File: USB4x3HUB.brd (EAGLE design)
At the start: 80 x 90 mm, 115 parts, among them IC1 TUSB2036, IC10 SN74LVC1G139DCTR, IC2 FSUSB74MPX, IC3 TPS2041C, IC4 TPS2041C, IC5 TPS2041C, IC6 3.3V, IC7 5V, IC8 5V, IC9 5V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

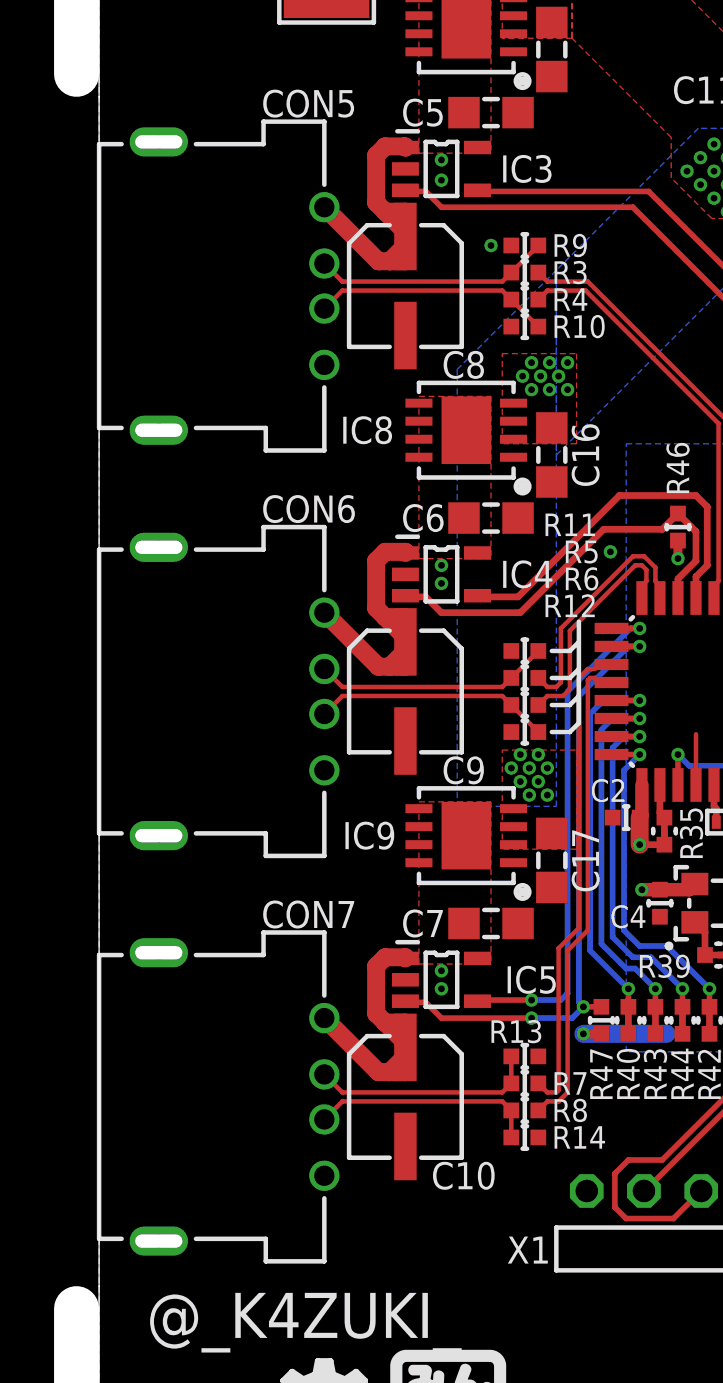
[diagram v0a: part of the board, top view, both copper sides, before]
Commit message: [ PCB ] library update and related fix
- CON5-7 pinout mistake fixed in library
  - move C8-10 to followw this change
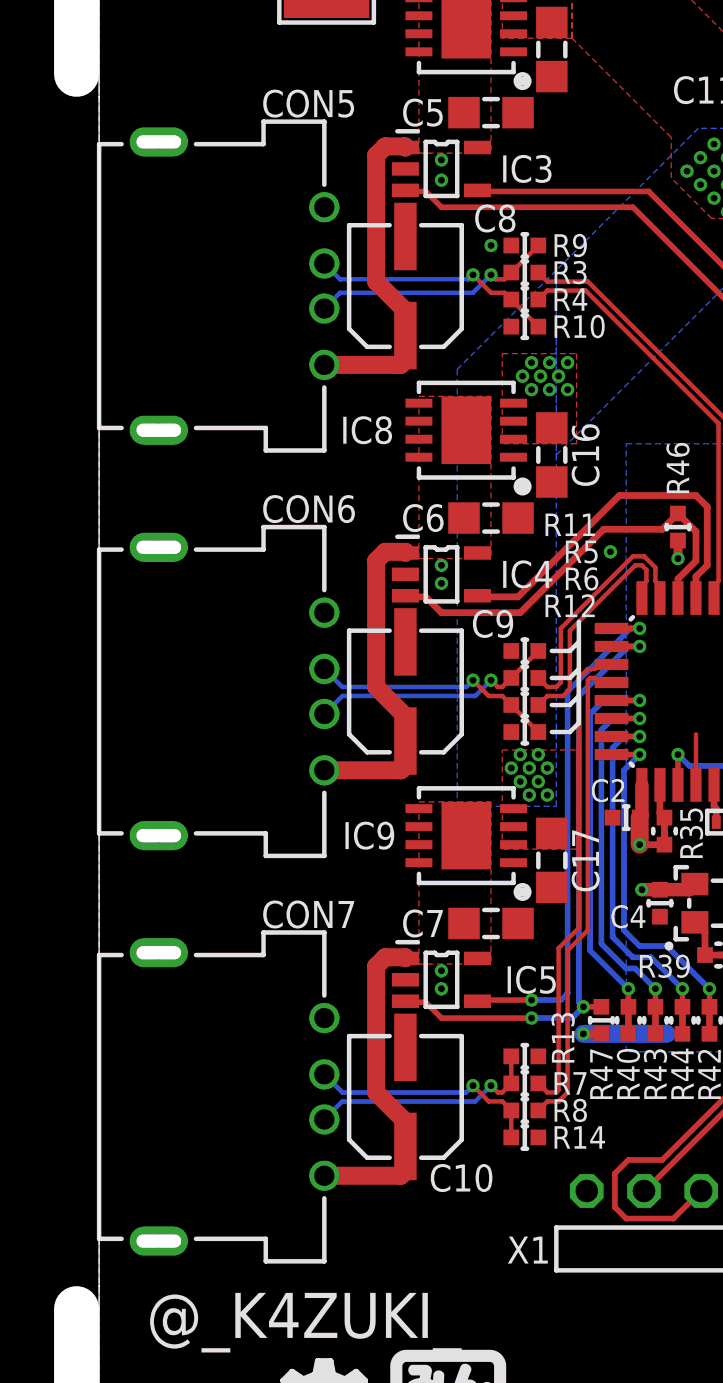
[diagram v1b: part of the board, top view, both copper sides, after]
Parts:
- turned C10 to 0 degrees
- turned C8 to 0 degrees
- turned C9 to 0 degrees
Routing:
- net N$12: track 14.1 -> 14.8 mm
- net N$13: track 14.1 -> 14.8 mm
- net N$11: track 14.2 -> 14.9 mm
- net N$27: track 10.00 -> 10.4 mm, vias 0 -> 1
- net N$26: track 10.00 -> 10.4 mm, vias 0 -> 1
- net N$23: track 10.5 -> 10.9 mm, vias 0 -> 1
- net N$22: track 10.5 -> 10.9 mm, vias 0 -> 1
- net N$19: track 10.5 -> 10.8 mm, vias 0 -> 1
- net N$18: track 10.5 -> 10.8 mm, vias 0 -> 1

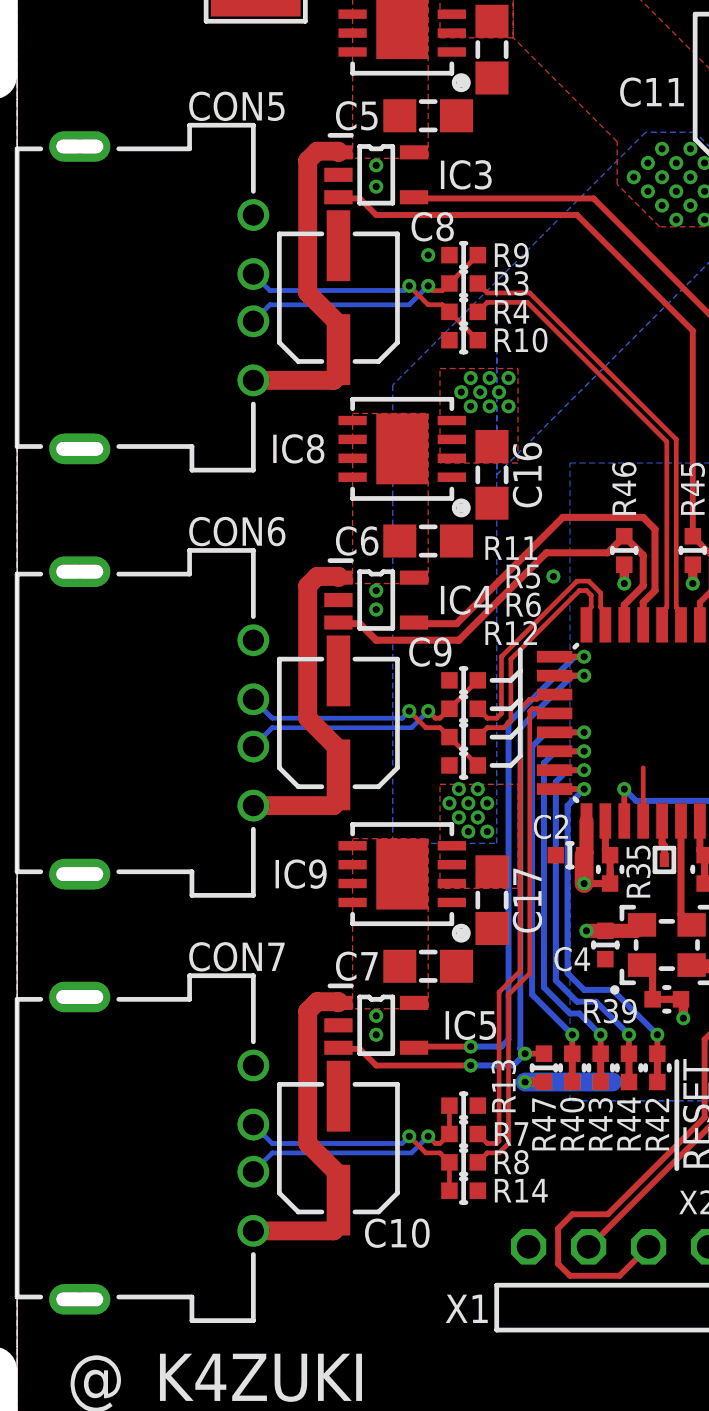
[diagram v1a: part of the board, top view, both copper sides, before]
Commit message: [ PCB ] move C8-10; shift USB downstream traces
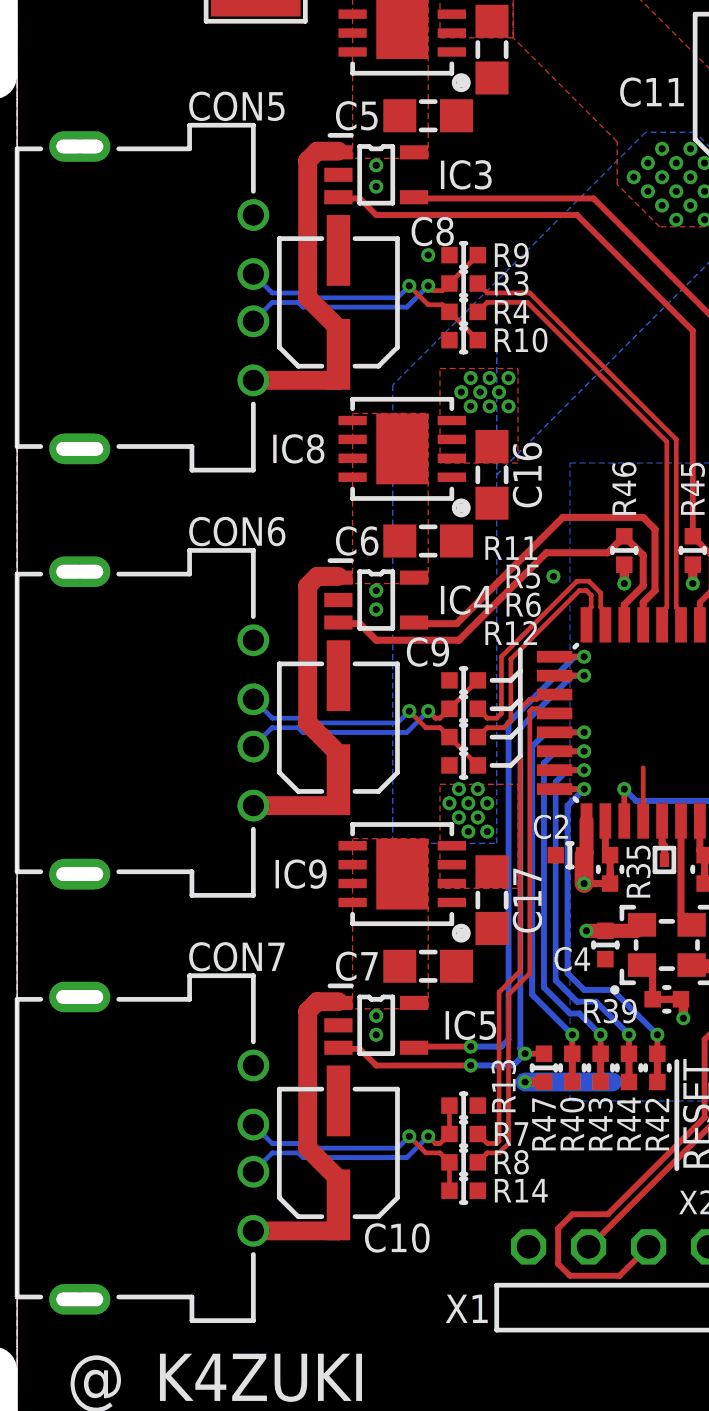
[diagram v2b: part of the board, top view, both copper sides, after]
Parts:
- moved C8 0.20 mm to (25.6, 62.8)
- moved C9 0.20 mm to (25.6, 44.8)
- moved C10 0.20 mm to (25.6, 26.8)

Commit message: [ BRD ] fix clock mode
- 48M source used while 6M source selected for IC
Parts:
- moved R38 0.10 mm to (41.0, 38.8)
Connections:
- net 3.3V: now also R38.1, R38.2
- net GND: no longer R38.1, R38.2
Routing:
- net 3.3V: track 63.7 -> 65.1 mm, vias 28 -> 29
- net GND: track 17.7 -> 16.4 mm
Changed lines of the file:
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@@
 <attribute name="VALUE" x="28.3" y="38.6" size="1.2" layer="27" ratio="17" rot="R90" align="center"/>
 </element>
-<element name="R38" library="mylib" package="R0402SHORT" value="" x="41.1" y="38.8" smashed="yes" rot="R90">
+<element name="R38" library="mylib" package="R0402SHORT" value="" x="41" y="38.8" smashed="yes" rot="R90">
 <attribute name="NAME" x="42.3" y="38.8" size="1" layer="25" font="vector" ratio="20" rot="R90" align="center"/>
-<attribute name="VALUE" x="41.1" y="38.8" size="1" layer="27" font="vector" rot="R90" align="center"/>
-<attribute name="NOT_COMPONENT" value="YES" x="41.1" y="38.8" size="1.778" layer="27" rot="R90" display="off"/>
+<attribute name="VALUE" x="41" y="38.8" size="1" layer="27" font="vector" rot="R90" align="center"/>
+<attribute name="NOT_COMPONENT" value="YES" x="41" y="38.8" size="1.778" layer="27" rot="R90" display="off"/>
 </element>
 <element name="TP100" library="mylib" package="FIDUCIAL" value="" x="5" y="15">
@@
 <contactref element="CON6" pad="4"/>
 <contactref element="CON7" pad="4"/>
-<contactref element="R38" pad="1"/>
 <contactref element="R40" pad="1"/>
 <contactref element="R43" pad="1"/>
@@
 <via x="34.7" y="51.2" extent="1-16" drill="0.3"/>
 <contactref element="R40" pad="2"/>
-<contactref element="R38" pad="2"/>
 <contactref element="R43" pad="2"/>
 <contactref element="R44" pad="2"/>
 <contactref element="R42" pad="2"/>
-<wire x1="41.1" y1="38.2" x2="41.1" y2="38.8" width="0.3" layer="1"/>
-<wire x1="41.1" y1="38.2" x2="41.8" y2="38.2" width="0.4" layer="1"/>
 </signal>
 <signal name="AVSS">
@@
 <contactref element="R39" pad="2"/>
 <wire x1="40.1" y1="33.3" x2="39.5" y2="33.3" width="0.3" layer="1"/>
+<contactref element="R38" pad="1"/>
+<contactref element="R38" pad="2"/>
+<via x="41.8" y="38.2" extent="1-16" drill="0.3"/>
+<wire x1="41" y1="38.2" x2="41.8" y2="38.2" width="0.25" layer="1"/>
+<wire x1="41" y1="38.2" x2="41" y2="38.8" width="0.25" layer="1"/>
 </signal>
 <signal name="N$15">
@@
 <contactref element="IC1" pad="31"/>
 <contactref element="R38" pad="3"/>
-<wire x1="40.9" y1="40.85" x2="40.9" y2="39.6" width="0.3" layer="1"/>
-<wire x1="40.9" y1="39.6" x2="41.1" y2="39.4" width="0.3" layer="1"/>
+<wire x1="40.9" y1="40.85" x2="40.9" y2="39.5" width="0.3" layer="1"/>
+<wire x1="40.9" y1="39.5" x2="41" y2="39.4" width="0.3" layer="1"/>
 </signal>
 <signal name="N$65">

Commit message: apply library updates; regenerate BOM
- add SMD_PAD/TH_PAD attributes
- update some supplier attributes
  - update BOM based on this update
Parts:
- C1, C13, C2, C22, C3, C4: value (none) -> 0.1u/1005
- GIT1: value 3d97858 -> 7236034
- Q1: value OSC4_48M -> OSC4_6.0M
- R10, R11, R12, R13, R14, R9: value (none) -> 15k/1005
- R24, R25, R31, R32, R33, R34, R37, R41, R45, R46, R47: value (none) -> 10k/1005
- R27, R28, R29, R30: value (none) -> 1k/1005
- moved R38 0.10 mm to (41.1, 38.8)
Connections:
- net 3.3V: no longer R38.1, R38.2
- net GND: now also R38.1, R38.2
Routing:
- net 3.3V: track 65.1 -> 63.7 mm, vias 29 -> 28

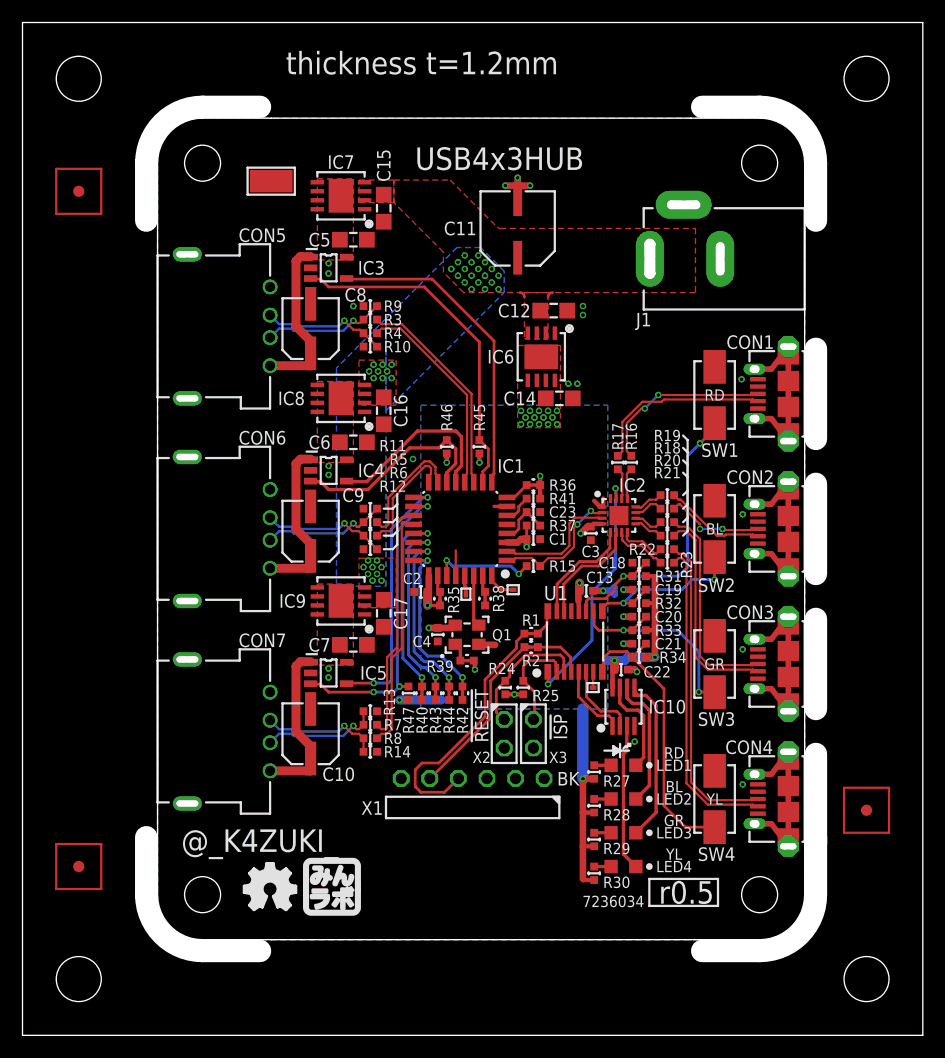
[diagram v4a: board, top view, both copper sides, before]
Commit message: [ BRD ] board width is 57.0mm
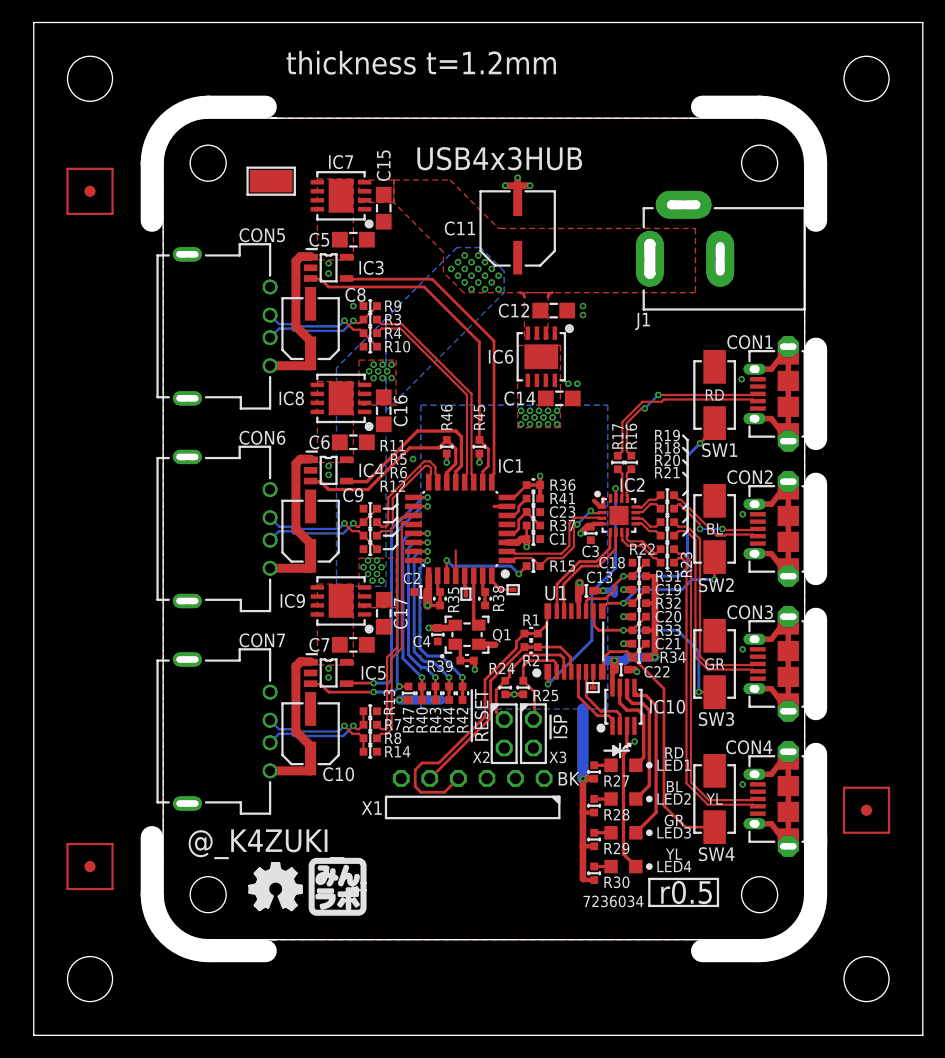
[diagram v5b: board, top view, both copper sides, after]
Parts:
- moved TP100 1.00 mm to (6.00, 15.0)
- moved TP102 1.00 mm to (6.00, 75.0)
- moved I1 0.50 mm to (25.5, 10.7)
- moved ICON1 0.50 mm to (22.5, 13.0)
- moved P1 0.50 mm to (16.5, 12.5)
- moved P2 0.50 mm to (16.5, 77.5)
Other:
- board size 80 x 90 mm -> 79 x 90 mm
- board text removed: "h=11"

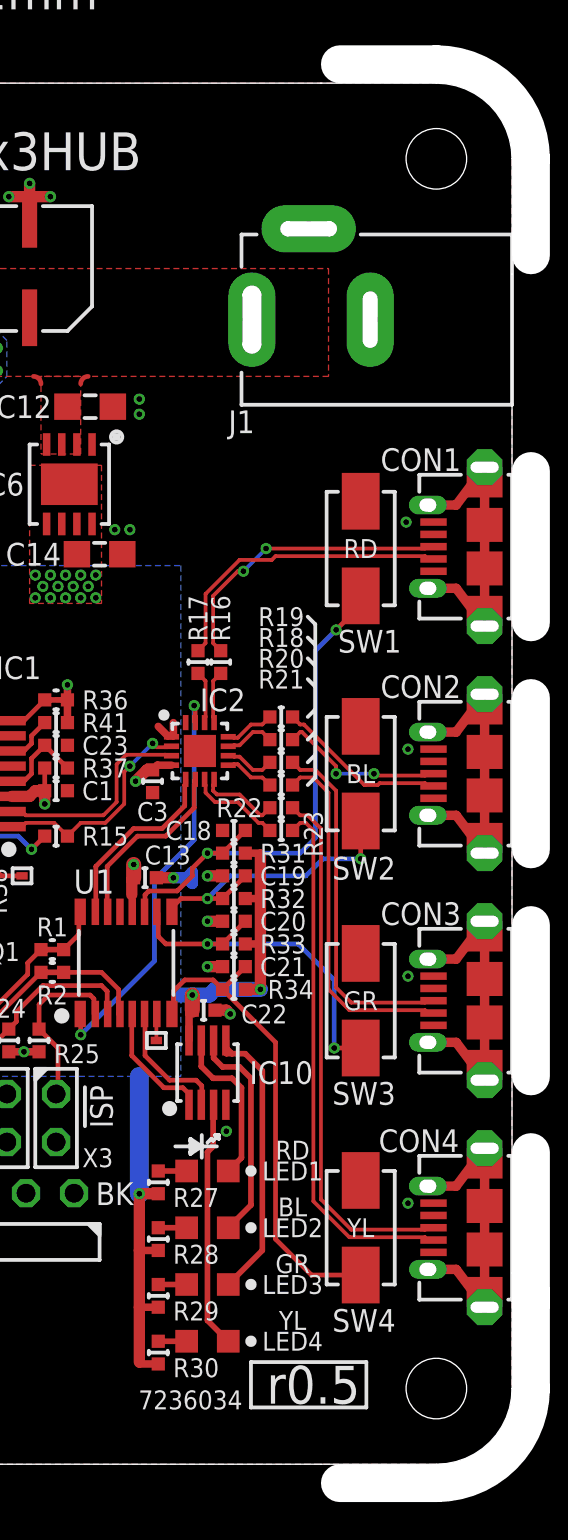
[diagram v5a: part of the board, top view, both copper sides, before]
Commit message: [BRD] replace SW1-4;add pin headers for daughter board
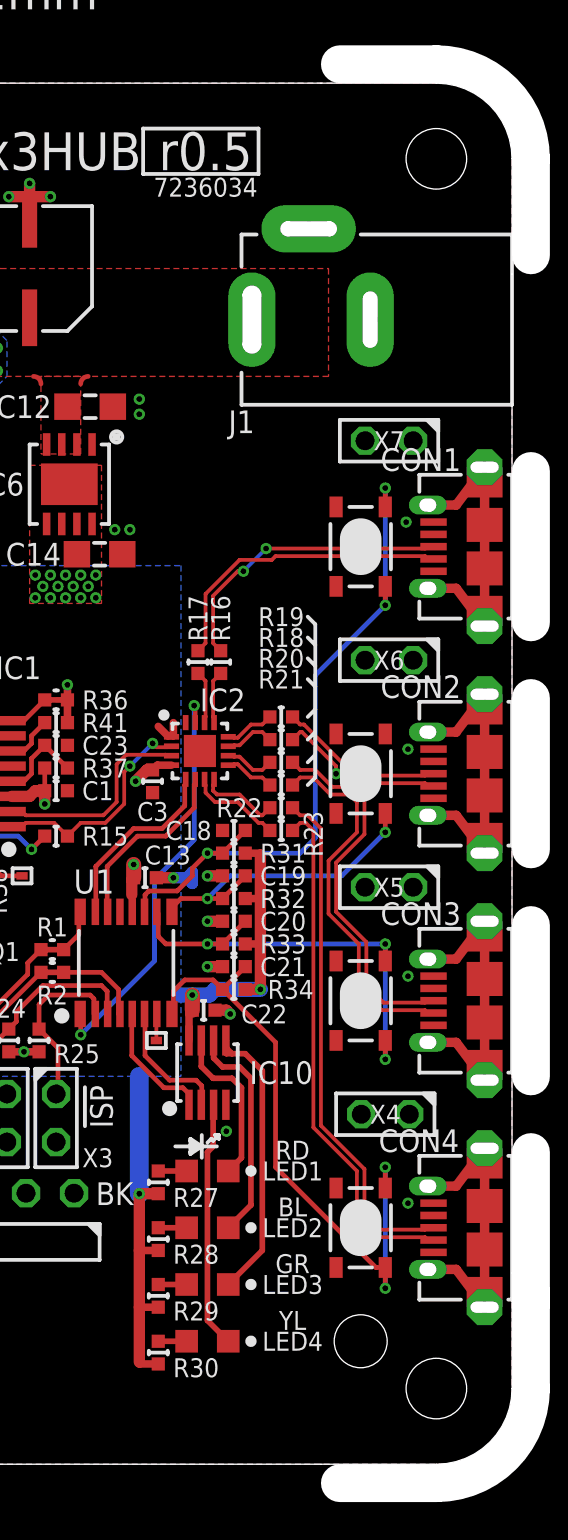
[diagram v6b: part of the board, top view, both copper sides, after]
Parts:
- added X4, X5, X6, X7: TSW-102-02-S-S, con-samtec.local:TSW-102-02-S-S
- SW1: value RD -> (none); device mylib:SW_TACTSW_FSM2JMTR -> mylib:SW_TACTSW_SKRPACE010
- SW2: value BL -> (none); device mylib:SW_TACTSW_FSM2JMTR -> mylib:SW_TACTSW_SKRPACE010
- SW3: value GR -> (none); device mylib:SW_TACTSW_FSM2JMTR -> mylib:SW_TACTSW_SKRPACE010
- SW4: value YL -> (none); device mylib:SW_TACTSW_FSM2JMTR -> mylib:SW_TACTSW_SKRPACE010
- moved ICON2 65.4 mm to (53.3, 77.9)
- moved GIT1 64.1 mm to (53.3, 76.0)
- moved SW1 0.10 mm to (61.5, 57.0), turned to 90 degrees
- turned SW2 to 90 degrees
- turned SW3 to 90 degrees
- turned SW4 to 90 degrees
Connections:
- net GND: now also SW1.2, SW2.2, SW3.2, SW4.2
- net SW1: now also SW1.3, SW1.4; no longer SW1.2
- net SW2: now also SW2.3, SW2.4; no longer SW2.2
- net SW3: now also SW3.3, SW3.4; no longer SW3.2
- net SW4: now also SW4.3, SW4.4; no longer SW4.2
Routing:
- net SW1: track 27.7 -> 35.9 mm, vias 2 -> 3
- net SW4: track 25.7 -> 33.2 mm, vias 0 -> 2
- net SW3: track 19.1 -> 24.0 mm, vias 2 -> 3
- net N$7: track 18.8 -> 19.8 mm
- net SW2: track 15.8 -> 16.7 mm
- net N$9: track 18.9 -> 19.7 mm
- net N$8: track 28.2 -> 27.6 mm
- net N$10: track 28.2 -> 27.6 mm
